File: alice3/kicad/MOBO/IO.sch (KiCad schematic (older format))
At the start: 22 parts, among them CON1 SD_Card, U1 MiniM4-D40, U2 LEVELCONVERTER, U3 LEVELCONVERTER, U4 LEVELCONVERTER, U5 LEVELCONVERTER, U6 Alice_3_bus, U7 DFROBOT_FTDI_BASIC, U8 LM2937-3.3, X1 MINI_DIN_6

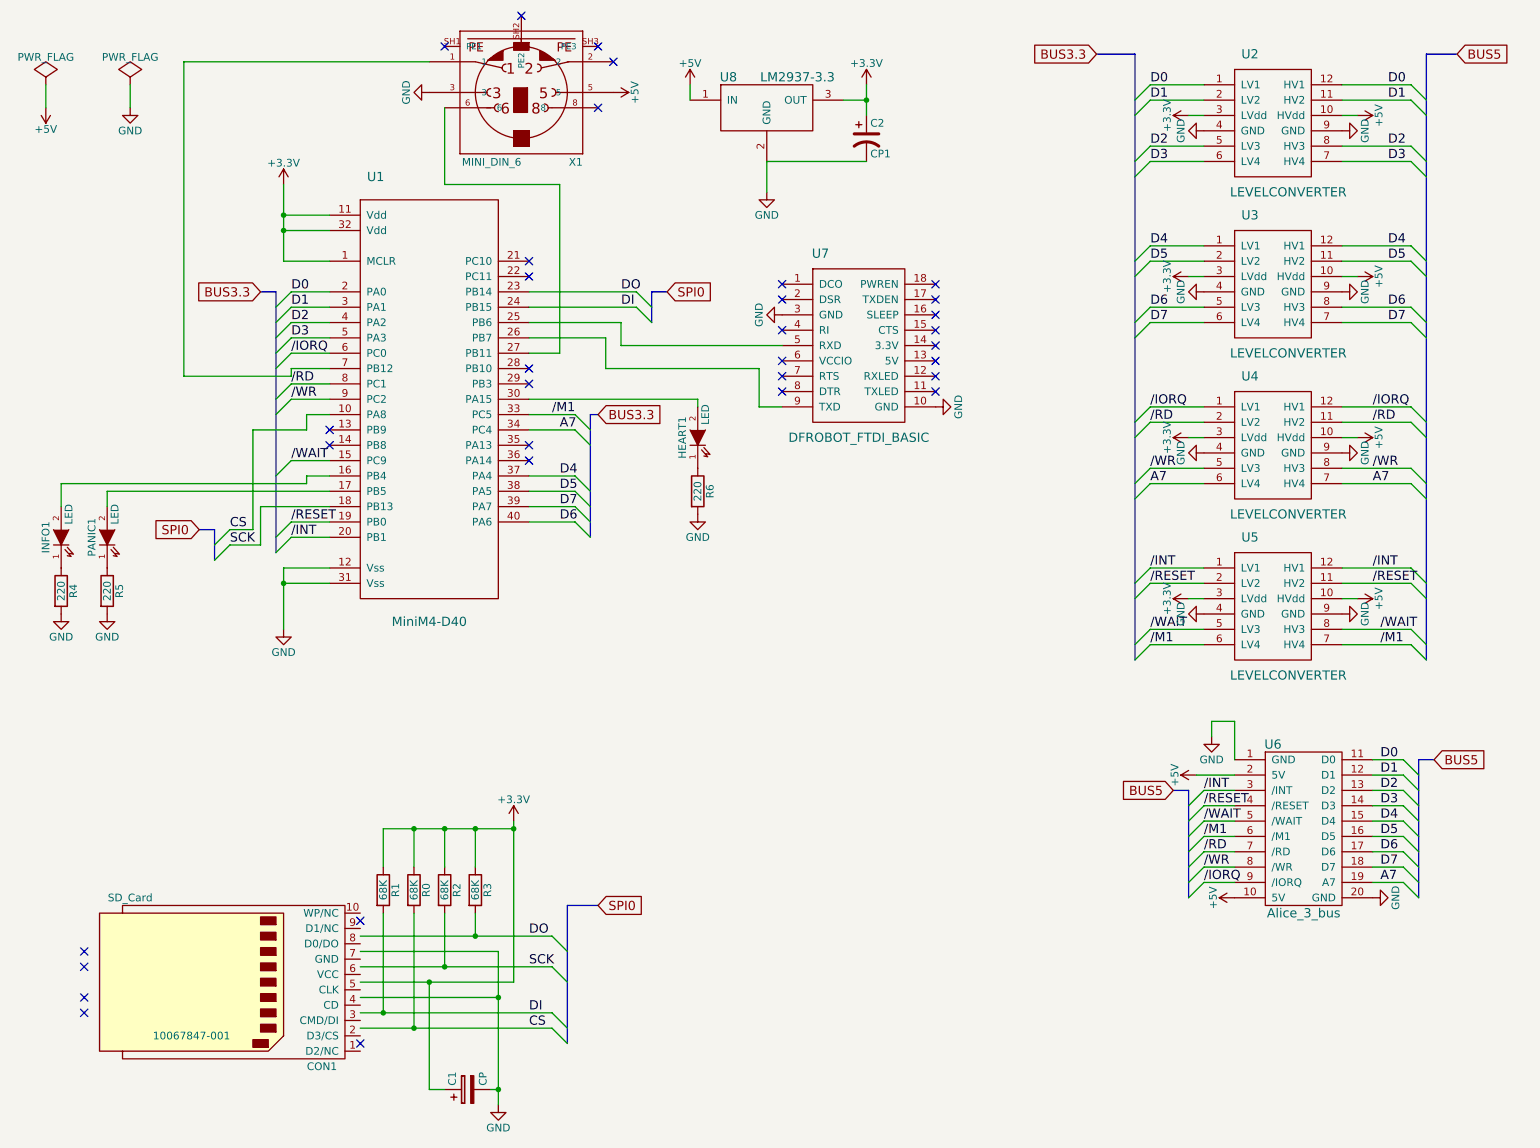
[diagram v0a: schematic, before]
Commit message: integrate as part of single board
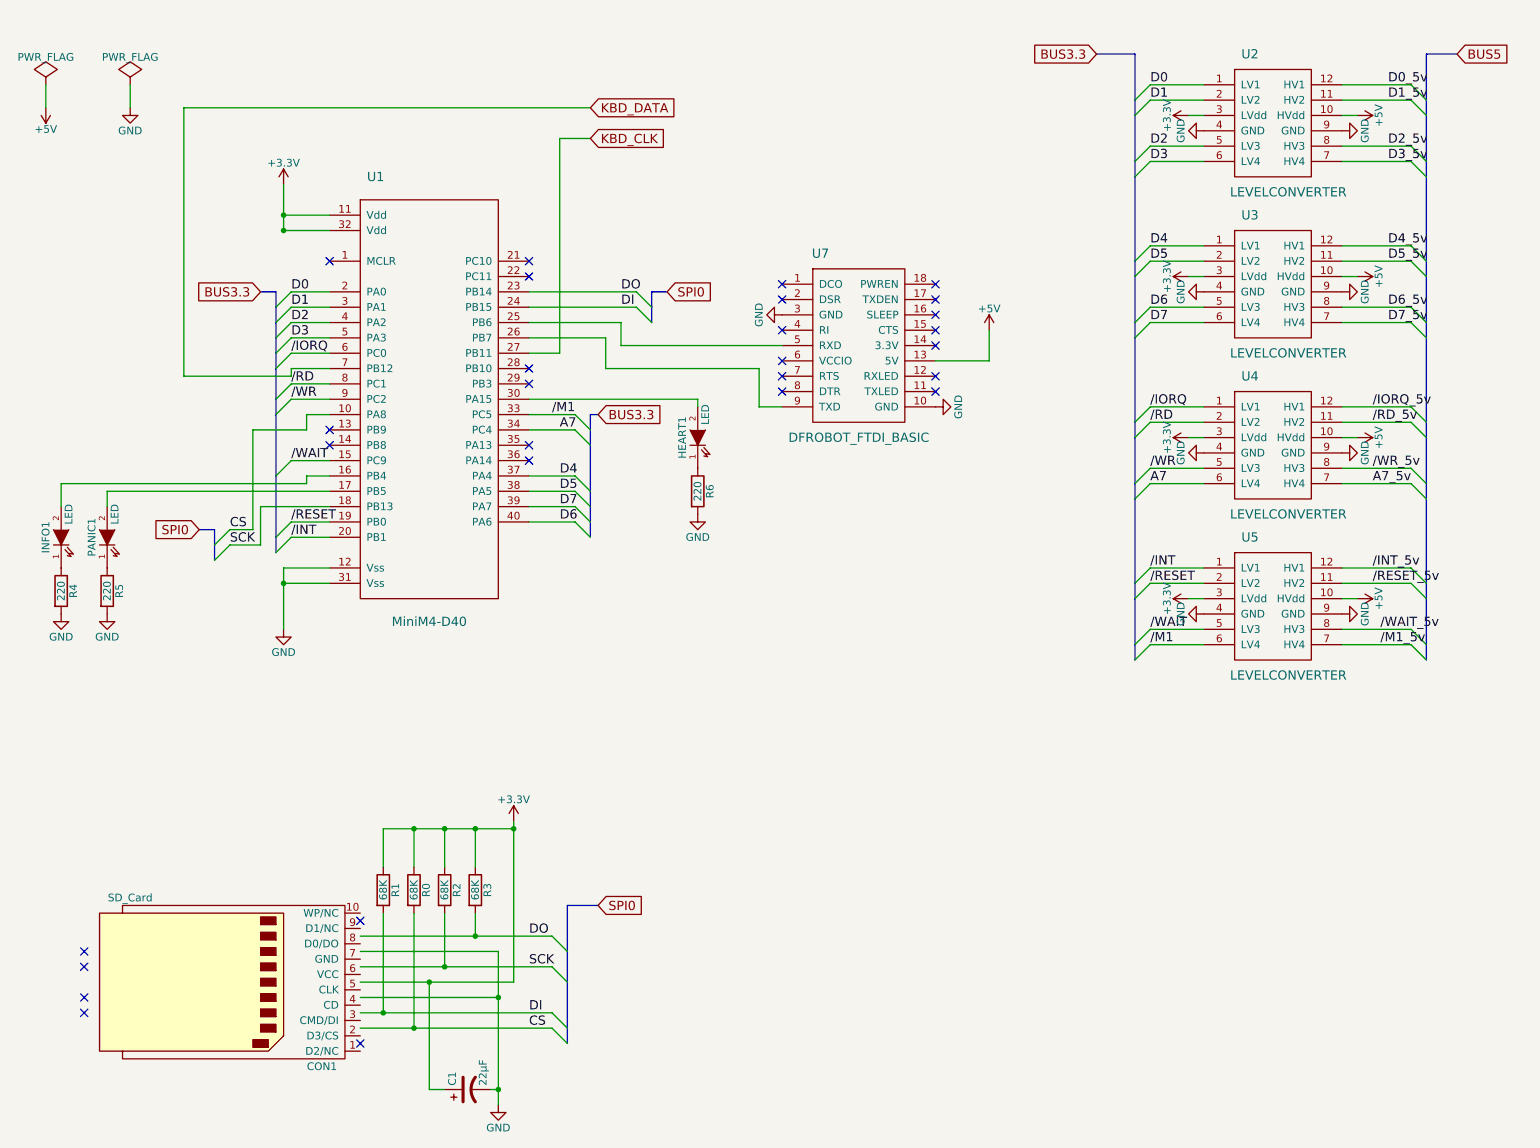
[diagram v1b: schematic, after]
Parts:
- removed C1: CP, symbol CP
- removed C2: CP1, symbol CP1
- removed U6: Alice_3_bus, symbol Alice_3_bus
- removed U8: LM2937-3.3, symbol LM2937-3.3
- removed X1: MINI_DIN_6, mini_din-M_DIN6, symbol MINI_DIN_6
- added C1: 22µF, Capacitors_ThroughHole:C_Radial_D5_L11_P2, symbol CP1
- CON1: footprint 10067847-001 -> Connect:SD_Card_Receptacle
- HEART1, INFO1, PANIC1: footprint (none) -> LEDs:LED-5MM
- R0, R1, R2, R3, R4, R5, R6: footprint (none) -> Resistors_ThroughHole:Resistor_Horizontal_RM10mm
- U1: footprint (none) -> Housings_DIP:DIP-40_W15.24mm
- U2, U3, U4, U5: footprint (none) -> level converter:LEVELCONV
- U7: footprint (none) -> ftdi basic breakout:FTDIBASIC
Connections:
- net labels added: /INT_5v, /IORQ_5v, /M1_5v, /RD_5v, /RESET_5v, /WAIT_5v, /WR_5v, A7_5v, D0_5v, D1_5v, D2_5v, D3_5v, D4_5v, D5_5v, D6_5v, D7_5v, KBD_CLK, KBD_DATA
- wire segments 146 -> 134
- no-connect marks 33 -> 28

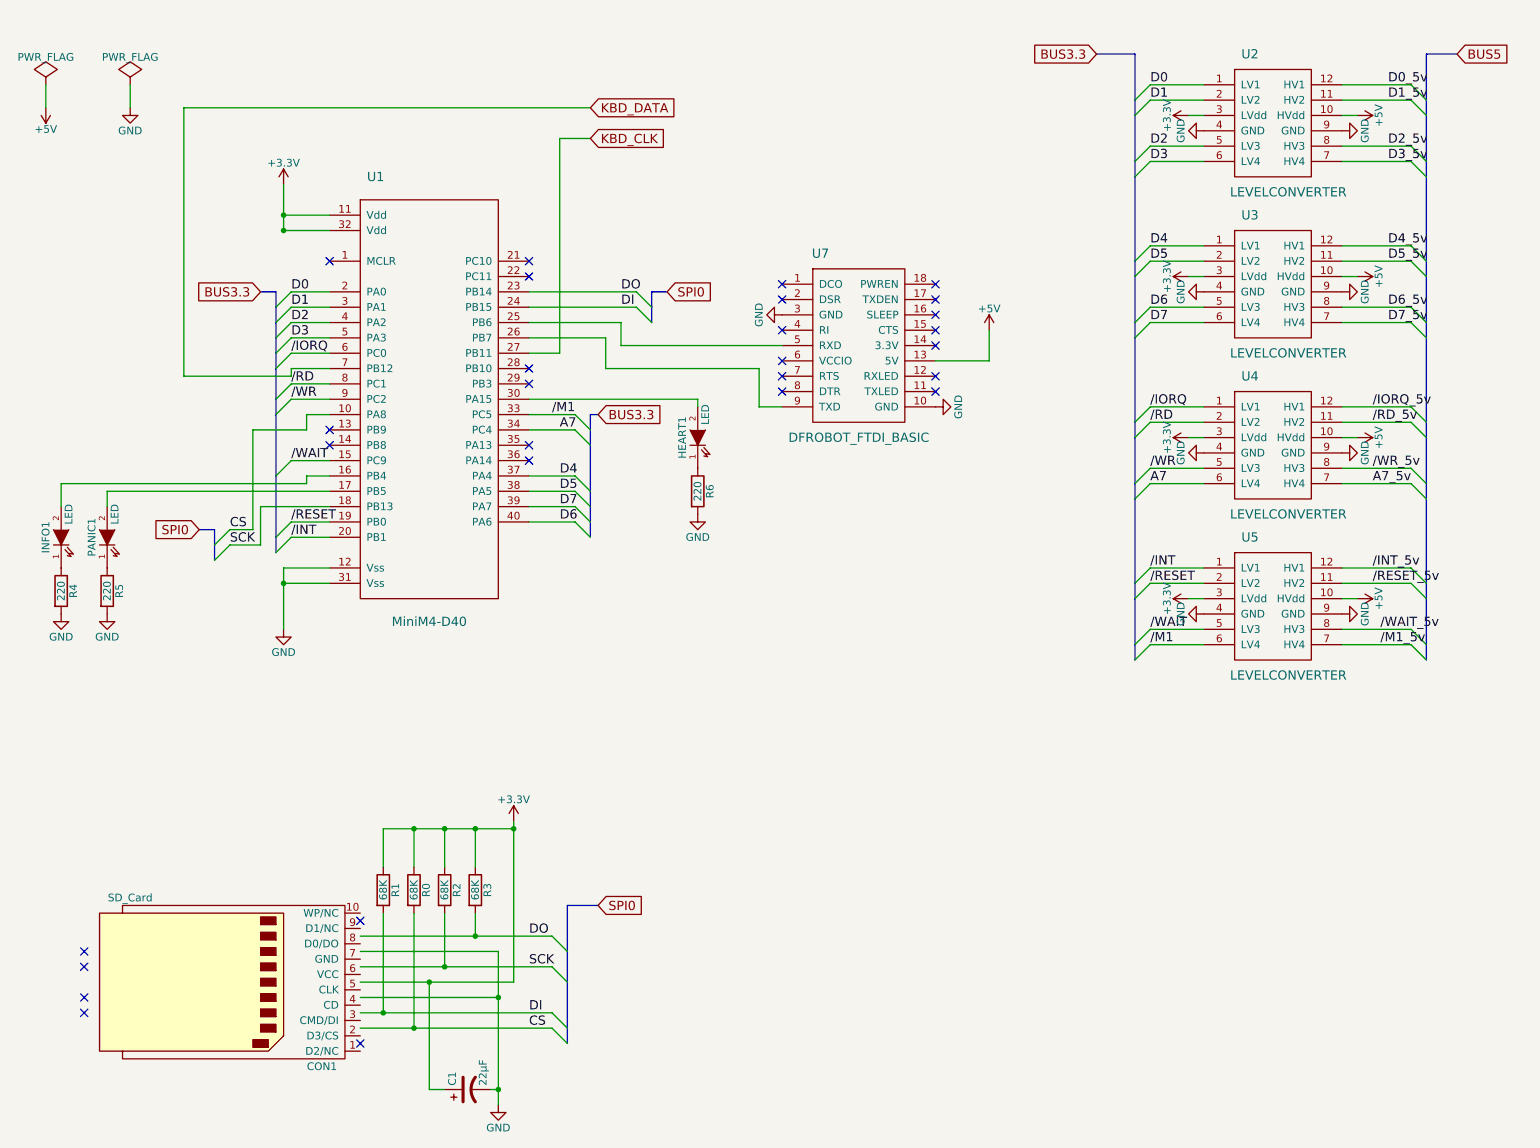
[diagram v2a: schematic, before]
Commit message: delete buses, add global labels
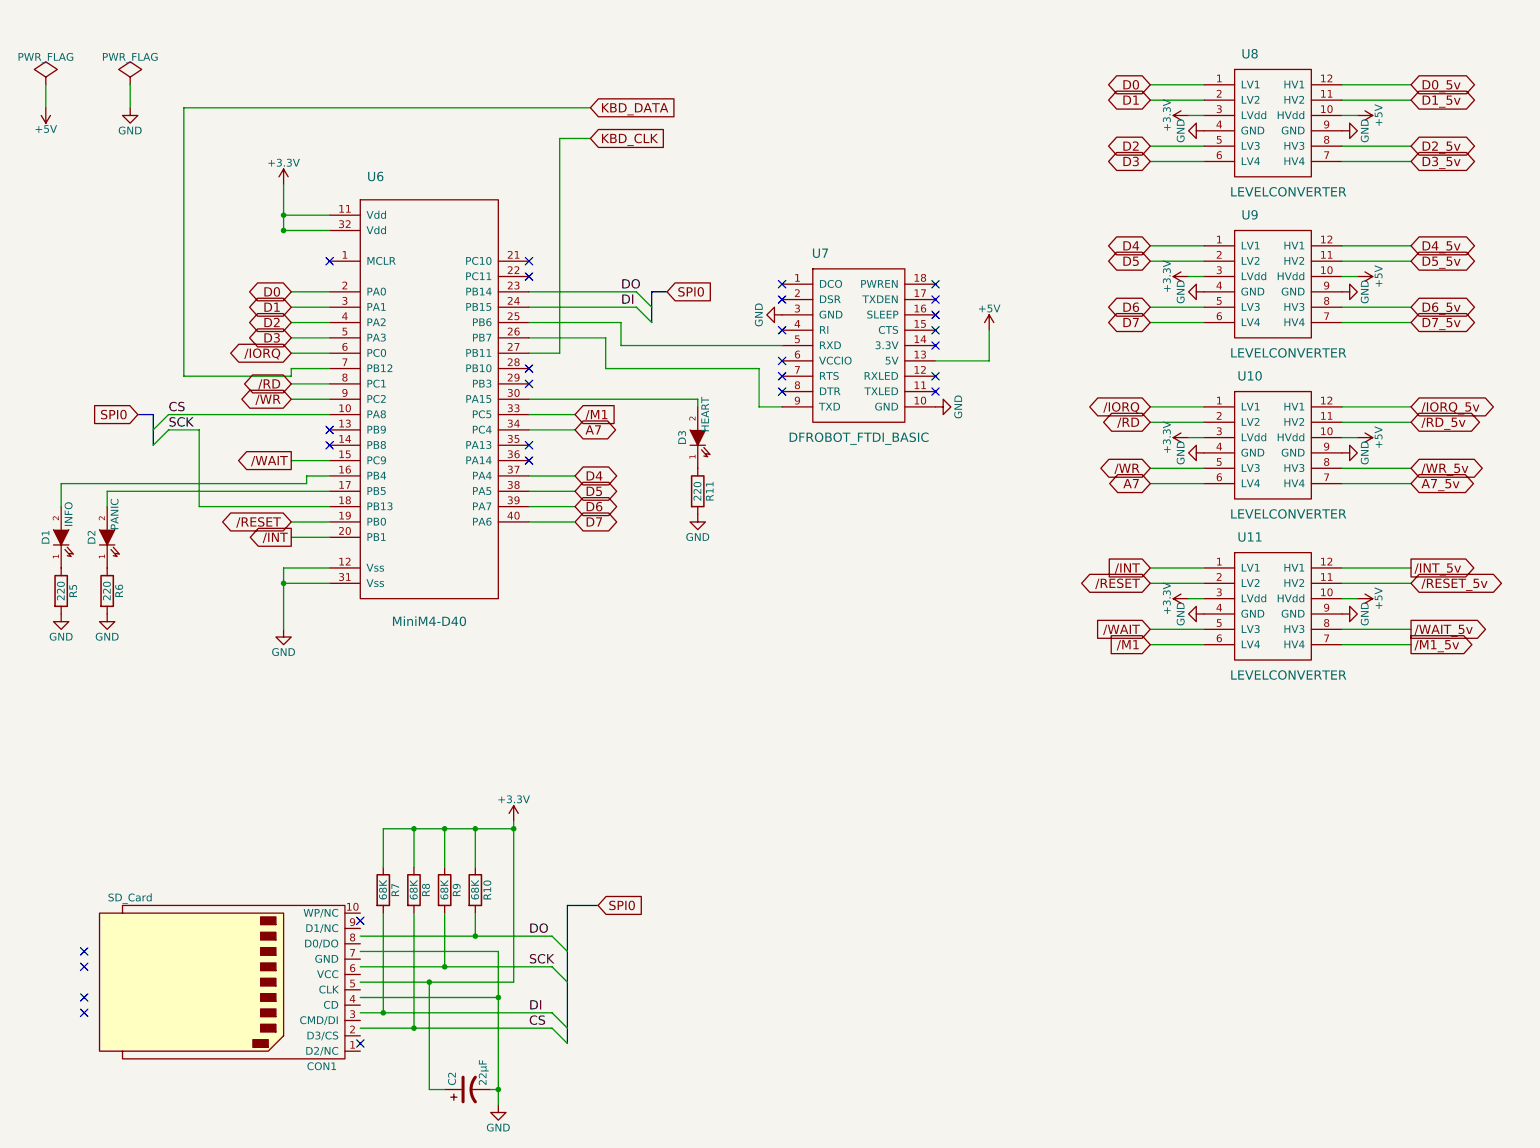
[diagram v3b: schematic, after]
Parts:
- D1: renamed from INFO1; value LED -> INFO
- D2: renamed from PANIC1; value LED -> PANIC
- D3: renamed from HEART1; value LED -> HEART
- renumbered C1 to C2, R3 to R10, R6 to R11, R4 to R5, R5 to R6, R1 to R7, R0 to R8, R2 to R9, U4 to U10, U5 to U11, U1 to U6, U2 to U8, U3 to U9
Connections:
- net labels removed: BUS3.3, BUS5
- wire segments 134 -> 117

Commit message: BUSRQ and BUSACK
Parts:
- added U?: LEVELCONVERTER, level converter:LEVELCONV, symbol LEVELCONVERTER
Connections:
- net labels added: /BUSACK, /BUSACK_5v, /BUSRQ, /BUSRQ_5v
- net labels removed: /M1_5v
- wire segments 117 -> 121
